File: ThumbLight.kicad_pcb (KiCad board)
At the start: 2 copper layers, 3 parts, among them U1 tp4056, U2 UA78M33_TO252, U3 ESP-12E

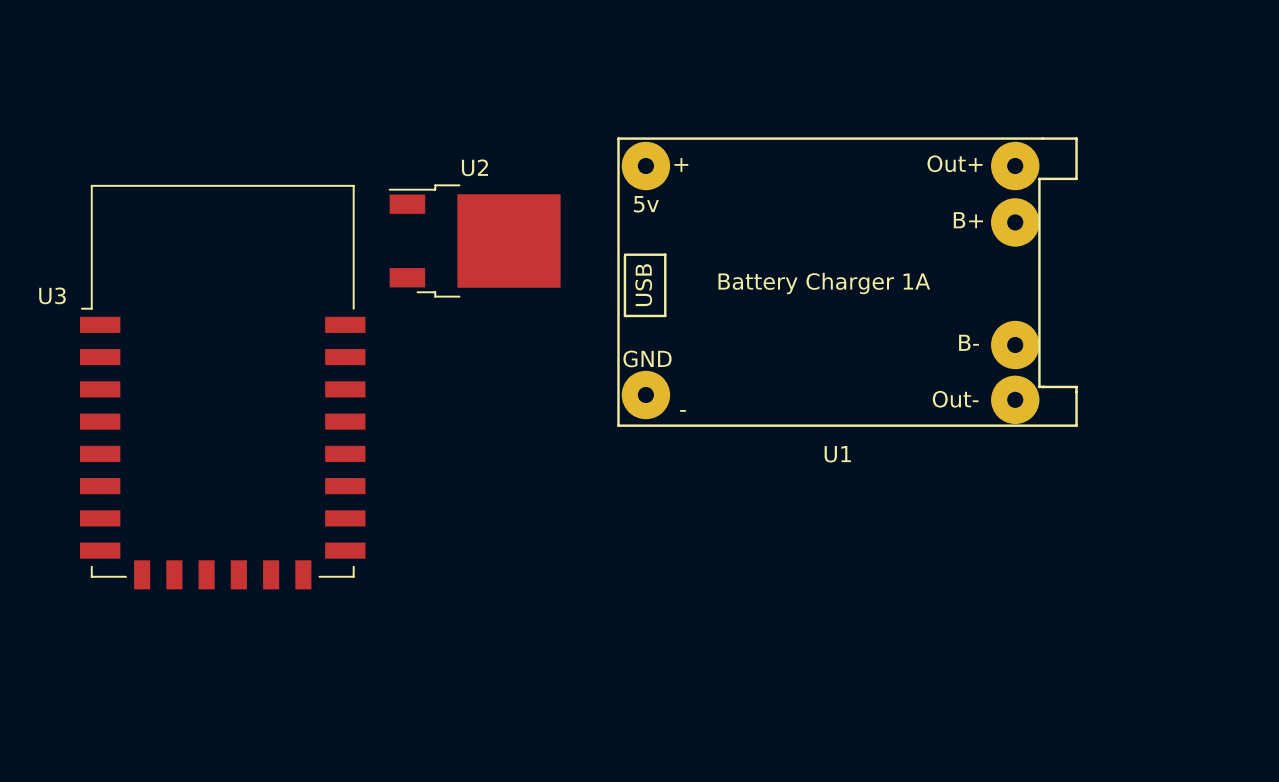
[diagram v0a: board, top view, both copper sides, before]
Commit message: Add FTDI component
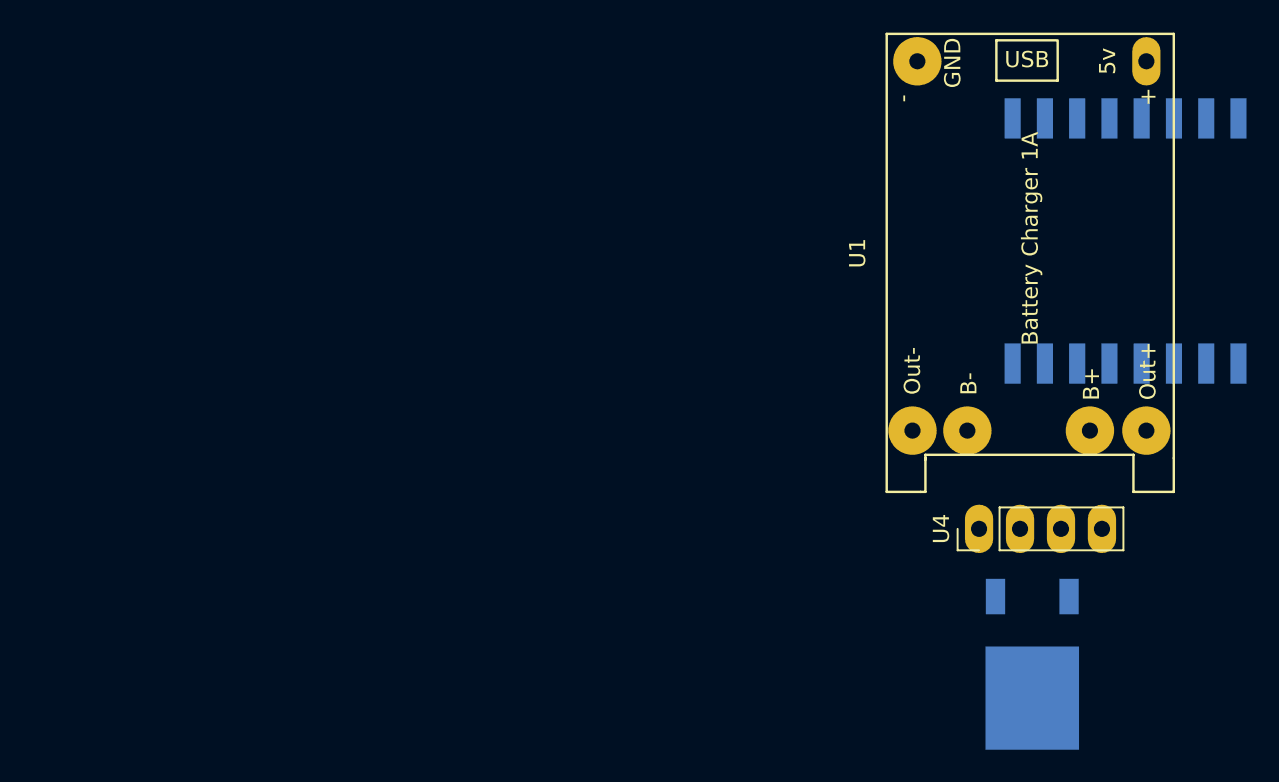
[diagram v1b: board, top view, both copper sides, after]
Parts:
- added U4: TTL, Connector_PinHeader_2.54mm:PinHeader_1x04_P2.54mm_Vertical, F.Cu at (169.7, 82.6)
- U2, U3: moved to B.Cu
- moved U3 53.2 mm to (175.3, 64.8), turned to -90 degrees
- moved U2 43.4 mm to (173.0, 91.0), turned to -90 degrees
- moved U1 35.0 mm to (181.8, 51.9), turned to -90 degrees
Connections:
- U3 pad 21: unconnected-(U3-Pad21) -> RX
- U3 pad 22: unconnected-(U3-Pad22) -> TX

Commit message: Add edges
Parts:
- moved U2 10.7 mm to (182.9, 87.0)
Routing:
- net +3V3: track 0.00 -> 28.0 mm
- net RX: track 0.00 -> 10.7 mm
- net TX: track 0.00 -> 10.4 mm
- net Net-(U1-Pad3): track 0.00 -> 6.50 mm
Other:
- board outline added: 27.3 x 53.3 mm
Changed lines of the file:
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@@
     (fp_line (start 0.4 11) (end 0.4 7.3) (layer "F.SilkS") (width 0.15))
     (fp_line (start 26.3 15.4) (end 28.4 15.4) (layer "F.SilkS") (width 0.15))
-    (pad "1" thru_hole oval (at 1.7 1.7 270) (size 3 1.75) (drill 1) (layers *.Cu *.Mask)
+    (pad "1" thru_hole circle (at 1.7 1.7 270) (size 1.7 1.7) (drill 1) (layers *.Cu *.Mask)
       (net 18 "+5V") (pinfunction "IN+") (pintype "power_in"))
-    (pad "2" thru_hole circle (at 1.7 15.9 270) (size 3 3) (drill 1) (layers *.Cu *.Mask)
+    (pad "2" thru_hole circle (at 1.7 15.9 270) (size 1.7 1.7) (drill 1) (layers *.Cu *.Mask)
       (net 2 "GND") (pinfunction "IN-") (pintype "power_in"))
-    (pad "3" thru_hole circle (at 24.6 1.7 270) (size 3 3) (drill 1) (layers *.Cu *.Mask)
+    (pad "3" thru_hole circle (at 24.6 1.7 270) (size 1.7 1.7) (drill 1) (layers *.Cu *.Mask)
       (net 1 "Net-(U1-Pad3)") (pinfunction "O+") (pintype "power_out"))
-    (pad "4" thru_hole circle (at 24.6 16.2 270) (size 3 3) (drill 1) (layers *.Cu *.Mask)
+    (pad "4" thru_hole circle (at 24.6 16.2 270) (size 1.7 1.7) (drill 1) (layers *.Cu *.Mask)
       (net 2 "GND") (pinfunction "O-") (pintype "power_out"))
-    (pad "5" thru_hole circle (at 24.6 5.2 270) (size 3 3) (drill 1) (layers *.Cu *.Mask)
+    (pad "5" thru_hole circle (at 24.6 5.2 270) (size 1.7 1.7) (drill 1) (layers *.Cu *.Mask)
       (net 19 "Net-(BT1-Pad1)") (pinfunction "B+") (pintype "power_in"))
-    (pad "6" thru_hole circle (at 24.6 12.8 270) (size 3 3) (drill 1) (layers *.Cu *.Mask)
+    (pad "6" thru_hole circle (at 24.6 12.8 270) (size 1.7 1.7) (drill 1) (layers *.Cu *.Mask)
       (net 20 "Net-(BT1-Pad2)") (pinfunction "B-") (pintype "power_in"))
     (model "${KIPRJMOD}/lib/tp4056/tp4056.step"
@@
   )
   (footprint "Package_TO_SOT_SMD:TO-252-2" (layer "B.Cu")
-    (at 172.975 91.015 -90)
+    (at 182.88 86.995 -90)
     (descr "TO-252 / DPAK SMD package, http://www.infineon.com/cms/en/product/packages/PG-TO252/PG-TO252-3-1/")
     (tags "DPAK TO-252 DPAK-3 TO-252-3 SOT-428")
@@
     )
   )
+  (gr_rect (start 178.1175 87.63) (end 166.0525 102.235) (layer "B.Cu") (width 0.2) (fill none))
+  (gr_poly
+    (pts
+      (xy 190.5 93.345)
+      (xy 179.07 93.345)
+      (xy 179.07 104.14)
+      (xy 166.37 104.14)
+      (xy 166.37 89.535)
+      (xy 163.195 89.535)
+      (xy 163.195 74.295)
+      (xy 170.18 74.295)
+      (xy 170.18 57.15)
+      (xy 163.195 57.15)
+      (xy 163.195 50.8)
+      (xy 190.5 50.8)
+    ) (layer "Edge.Cuts") (width 0.2) (fill none))
+  (segment (start 180.050414 76.5275) (end 180.6 77.077086) (width 0.6) (layer "B.Cu") (net 1))
+  (segment (start 180.6 77.077086) (end 180.6 82.795) (width 0.6) (layer "B.Cu") (net 1))
+  (segment (start 188.335 59.745) (end 188.335 79.62) (width 0.6) (layer "B.Cu") (net 3))
+  (segment (start 188.335 79.62) (end 185.16 82.795) (width 0.6) (layer "B.Cu") (net 3))
+  (segment (start 185.76 57.17) (end 188.335 59.745) (width 0.6) (layer "B.Cu") (net 3))
+  (segment (start 174.756776 82.619707) (end 174.756776 81.741635) (width 0.6) (layer "B.Cu") (net 16))
+  (segment (start 173.76 80.744859) (end 173.76 72.37) (width 0.6) (layer "B.Cu") (net 16))
+  (segment (start 174.756776 81.741635) (end 173.76 80.744859) (width 0.6) (layer "B.Cu") (net 16))
+  (segment (start 171.76 72.37) (end 171.76 82.162931) (width 0.6) (layer "B.Cu") (net 17))
+  (segment (start 171.76 82.162931) (end 172.216776 82.619707) (width 0.6) (layer "B.Cu") (net 17))
 )

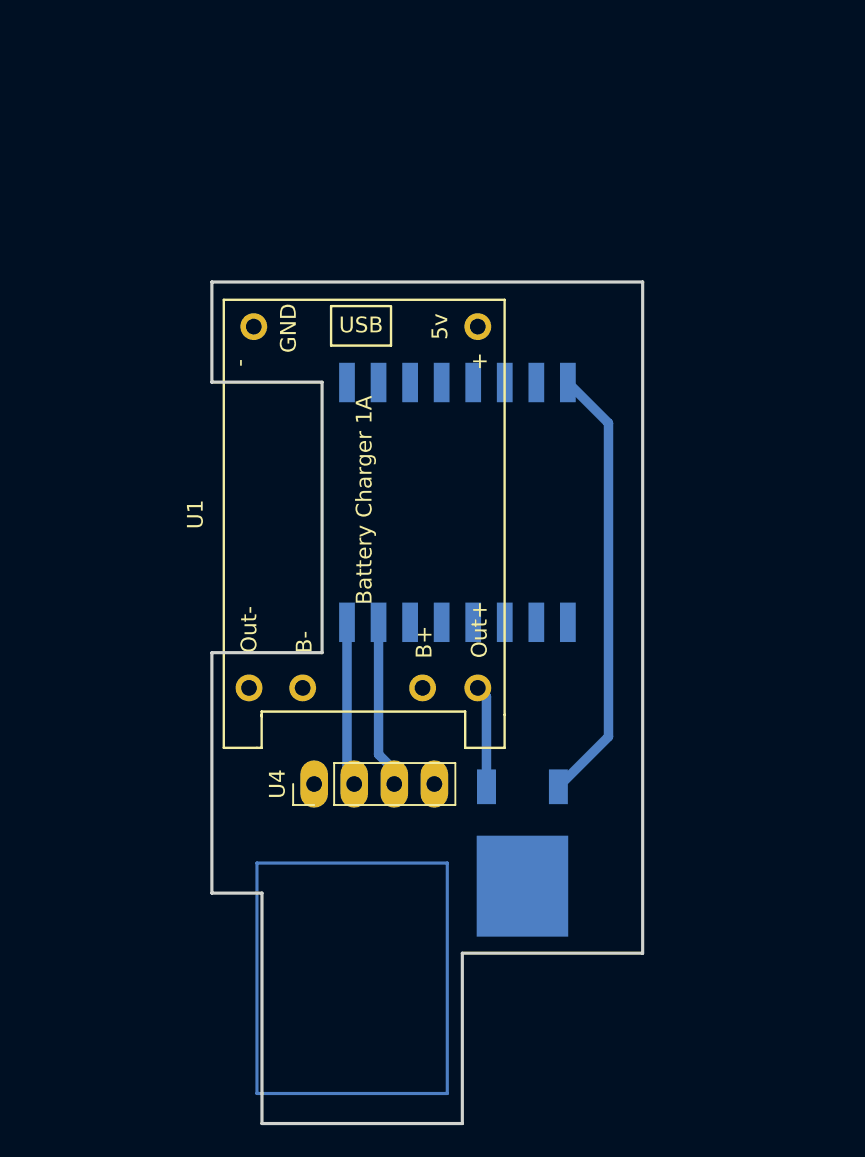
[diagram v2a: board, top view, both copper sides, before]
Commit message: rough layout and remove battery functionality
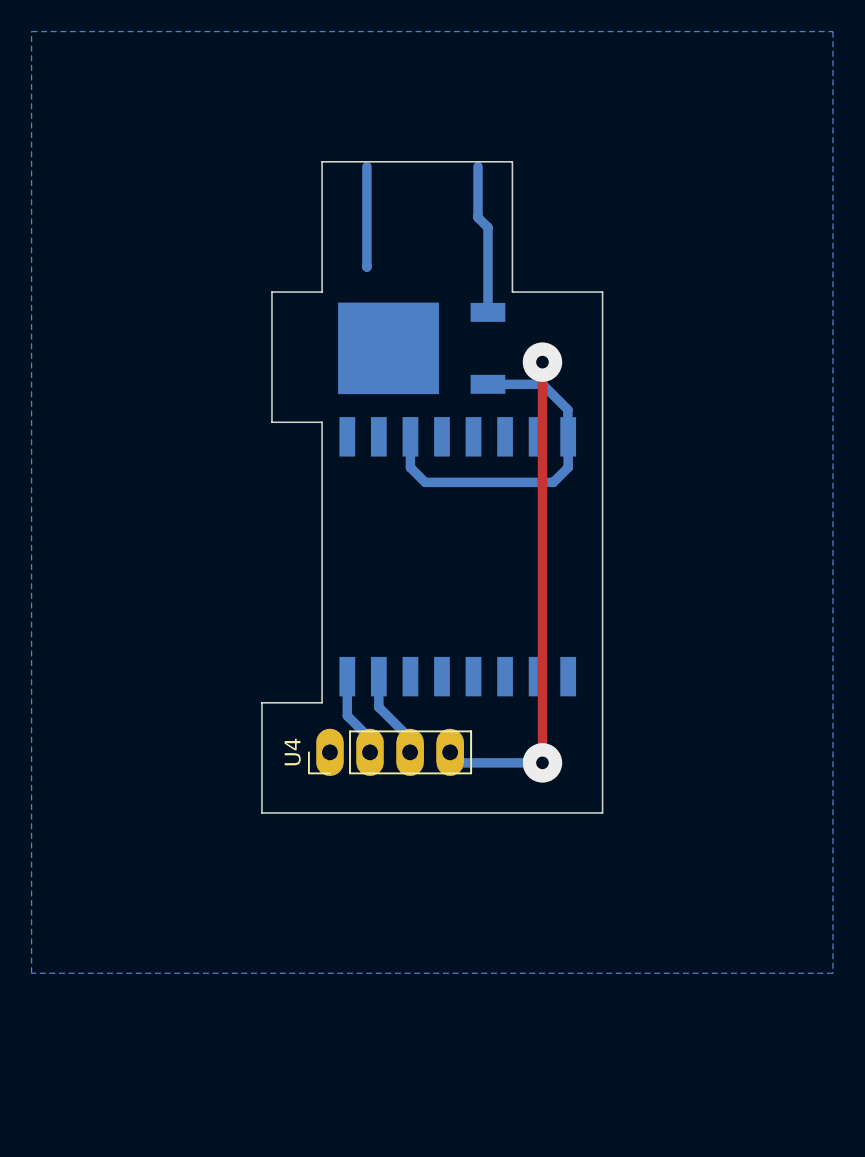
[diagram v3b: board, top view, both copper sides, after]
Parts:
- removed U1: tp4056, tp4056:tp4056
- moved U2 32.6 mm to (176.5, 55.0), turned to 180 degrees
- moved U3 3.44 mm to (175.3, 68.2)
- moved U4 2.24 mm to (170.7, 80.6)
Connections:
- U2 pad 1: Net-(U1-Pad3) -> +5V
- U3 pad 16: unconnected-(U3-Pad16) -> GND
- U3 pad 3: unconnected-(U3-Pad3) -> +3V3
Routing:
- net +3V3: track 28.0 -> 55.1 mm, vias 0 -> 2
- net +5V: track 0.00 -> 9.51 mm
- net Net-(U1-Pad3): track 6.50 -> 0.00 mm
- net GND: track 0.00 -> 6.38 mm
- net TX: track 10.4 -> 5.40 mm
- net RX: track 10.7 -> 5.62 mm
- added copper zone on B.Cu, net GND
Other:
- board size 27.3 x 53.3 mm -> 21.6 x 41.3 mm

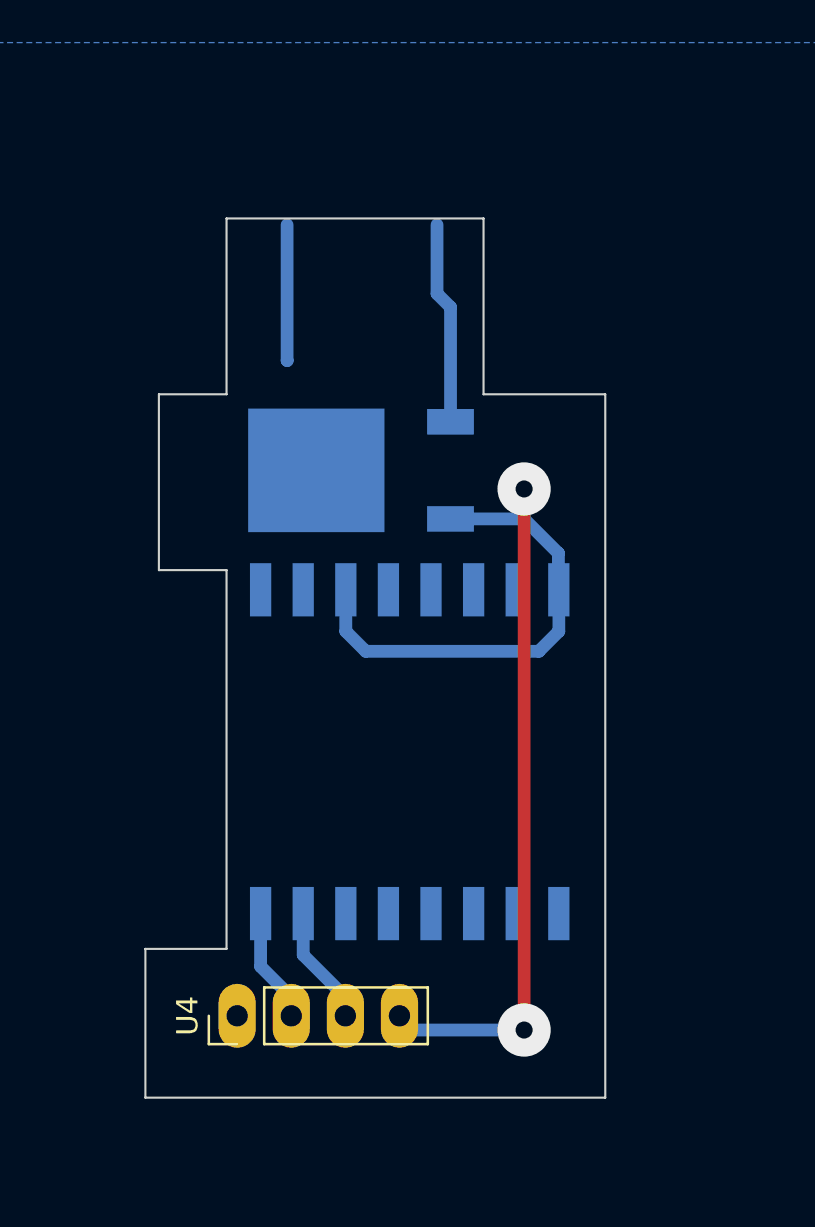
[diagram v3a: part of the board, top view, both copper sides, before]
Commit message: Add PROGRAM Jumper as well as a DHT11 sensor
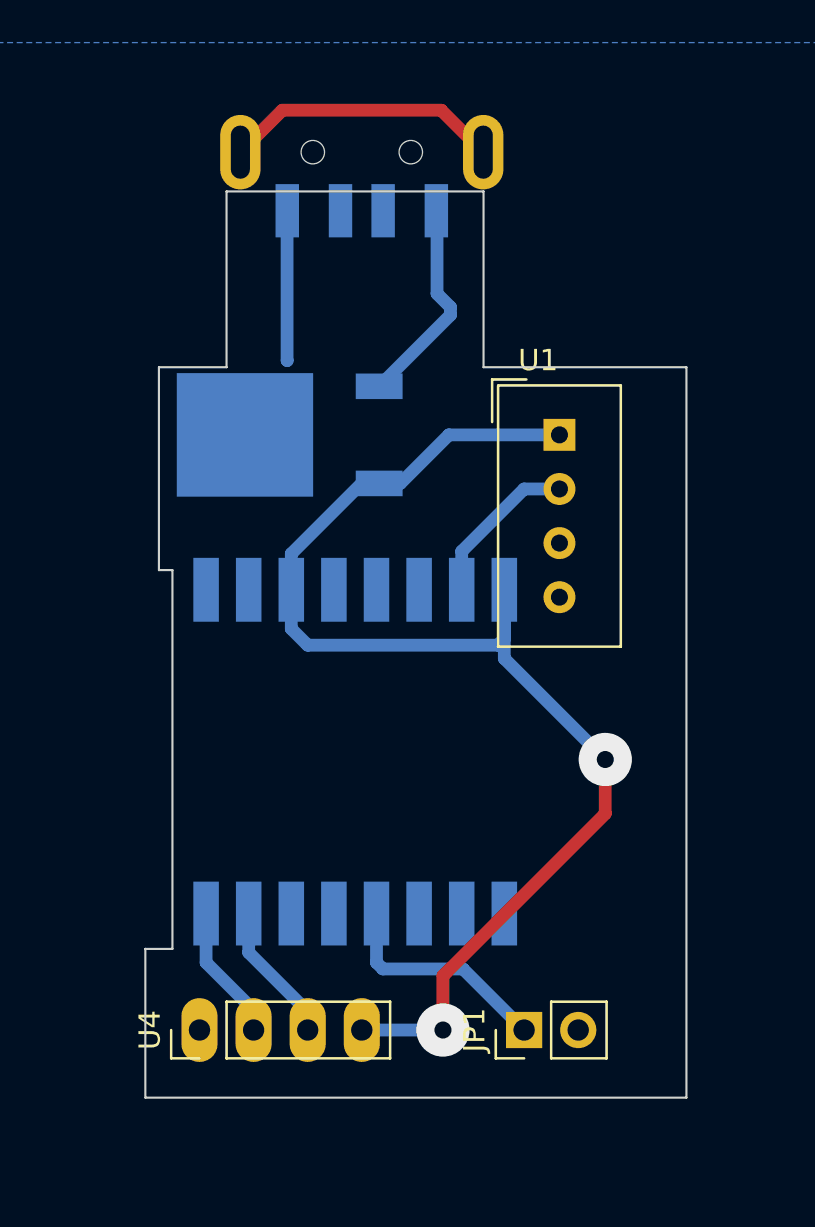
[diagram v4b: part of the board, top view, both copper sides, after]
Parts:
- added J1: USB_A, Connector_USB:USB_A_CNCTech_1001-011-01101_Horizontal, B.Cu at (176.5, 33.2)
- added JP1: PROG, Connector_PinHeader_2.54mm:PinHeader_1x02_P2.54mm_Vertical, F.Cu at (184.2, 81.3)
- added U1: DHT11, Sensor:Aosong_DHT11_5.5x12.0_P2.54mm, F.Cu at (185.8, 53.3)
- moved U2 3.74 mm to (173.1, 53.3)
- moved U3 2.56 mm to (172.7, 68.2)
- moved U4 1.89 mm to (168.9, 81.3)
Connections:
- U3 pad 18: unconnected-(U3-Pad18) -> Net-(U3-Pad18)
- U3 pad 7: unconnected-(U3-Pad7) -> TEMP
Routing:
- net unconnected-(J1-Pad5): track 0.00 -> 13.0 mm
- net Net-(U3-Pad18): track 0.00 -> 10.5 mm
- net TEMP: track 0.00 -> 7.78 mm
- net +3V3: track 55.1 -> 60.9 mm
- net TX: track 5.40 -> 6.39 mm
- net RX: track 5.62 -> 6.61 mm
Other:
- board size 21.6 x 41.3 mm -> 25.4 x 42.5 mm
- board text added: "COVER!"

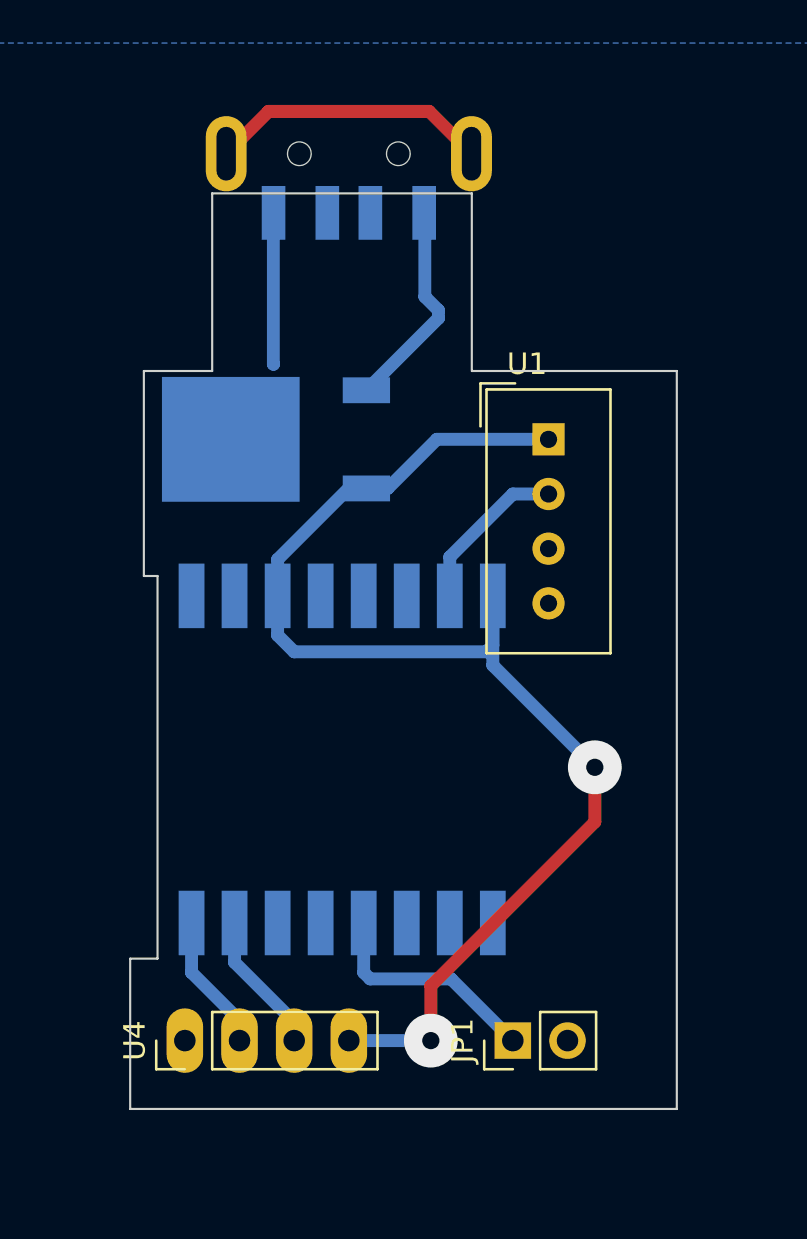
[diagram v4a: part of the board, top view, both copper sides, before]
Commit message: Add USB Footprint
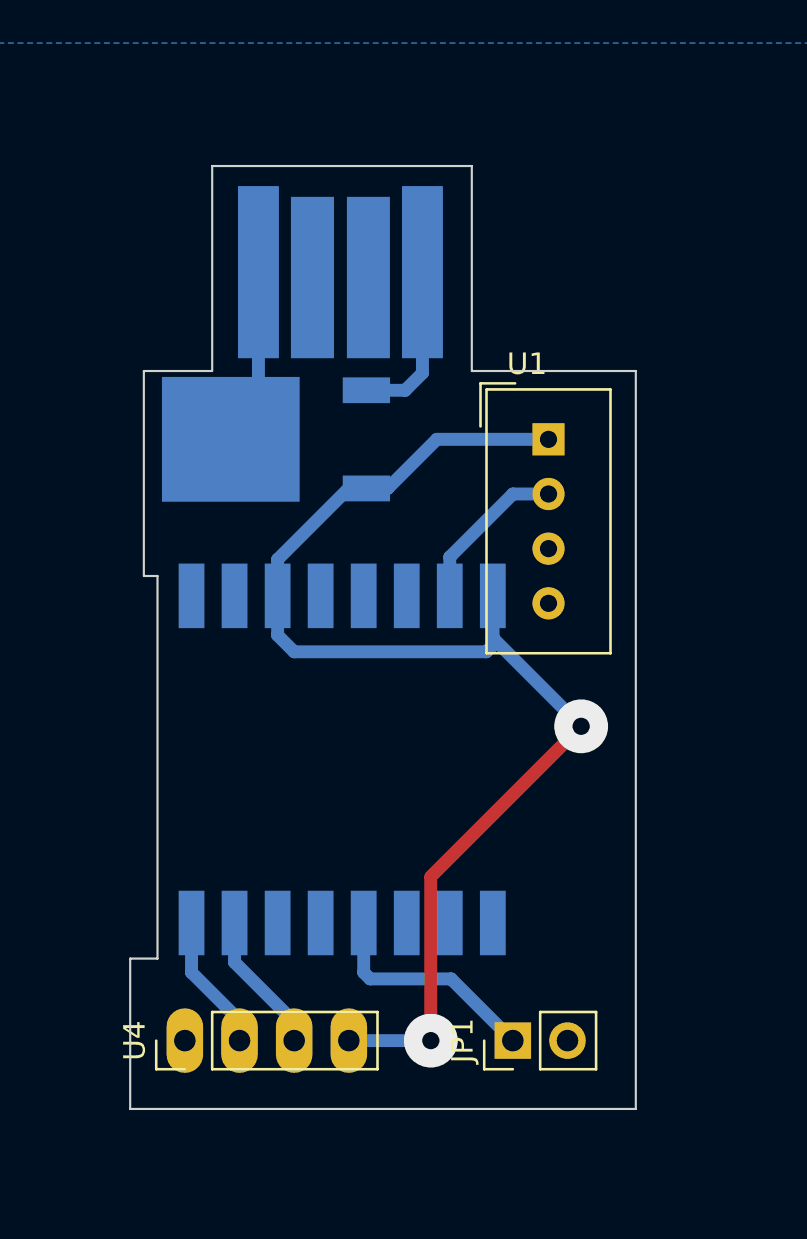
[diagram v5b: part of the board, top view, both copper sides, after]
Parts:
- J1: footprint Connector_USB:USB_A_CNCTech_1001-011-01101_Horizontal -> usb-a-pcb:usb-a-pcb
- moved J1 20.3 mm to (182.1, 52.7), turned to 180 degrees
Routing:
- net unconnected-(J1-Pad5): track 13.0 -> 0.00 mm
- net GND: track 6.38 -> 8.30 mm
- net +5V: track 9.23 -> 7.63 mm
- net +3V3: track 60.9 -> 60.4 mm
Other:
- board size 25.4 x 42.5 mm -> 23.5 x 43.8 mm
